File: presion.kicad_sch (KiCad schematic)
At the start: 7 parts, among them J6 Sens. Presión, U7 LM358

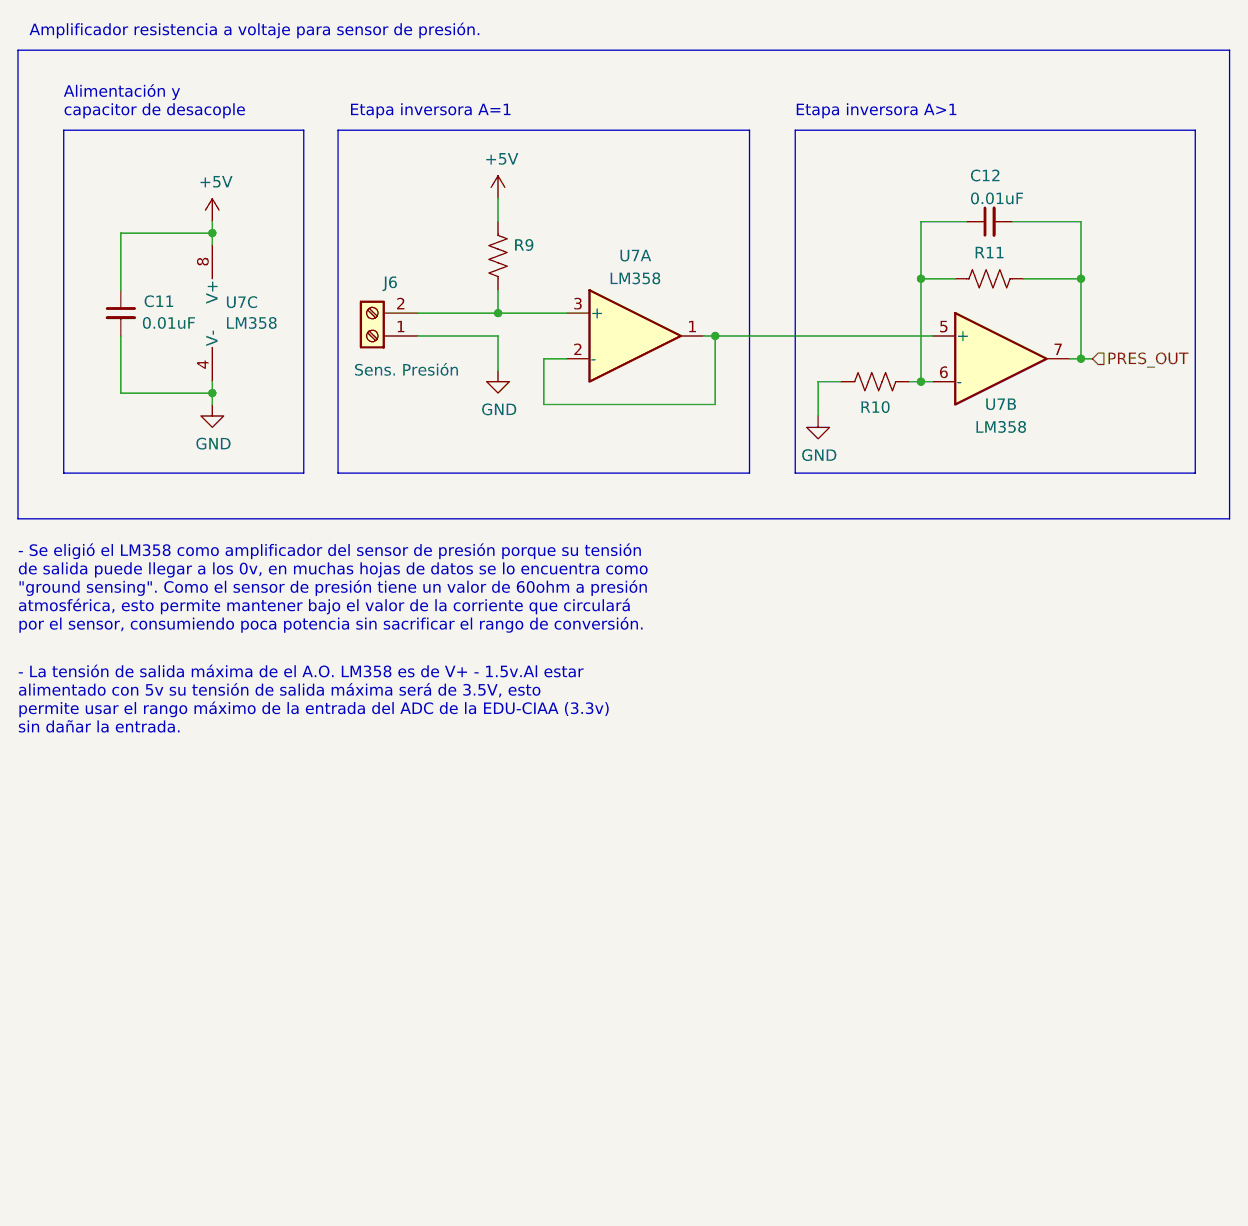
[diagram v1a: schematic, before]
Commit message: Cambios en plano de presion y agregue render en 3D de la placa.
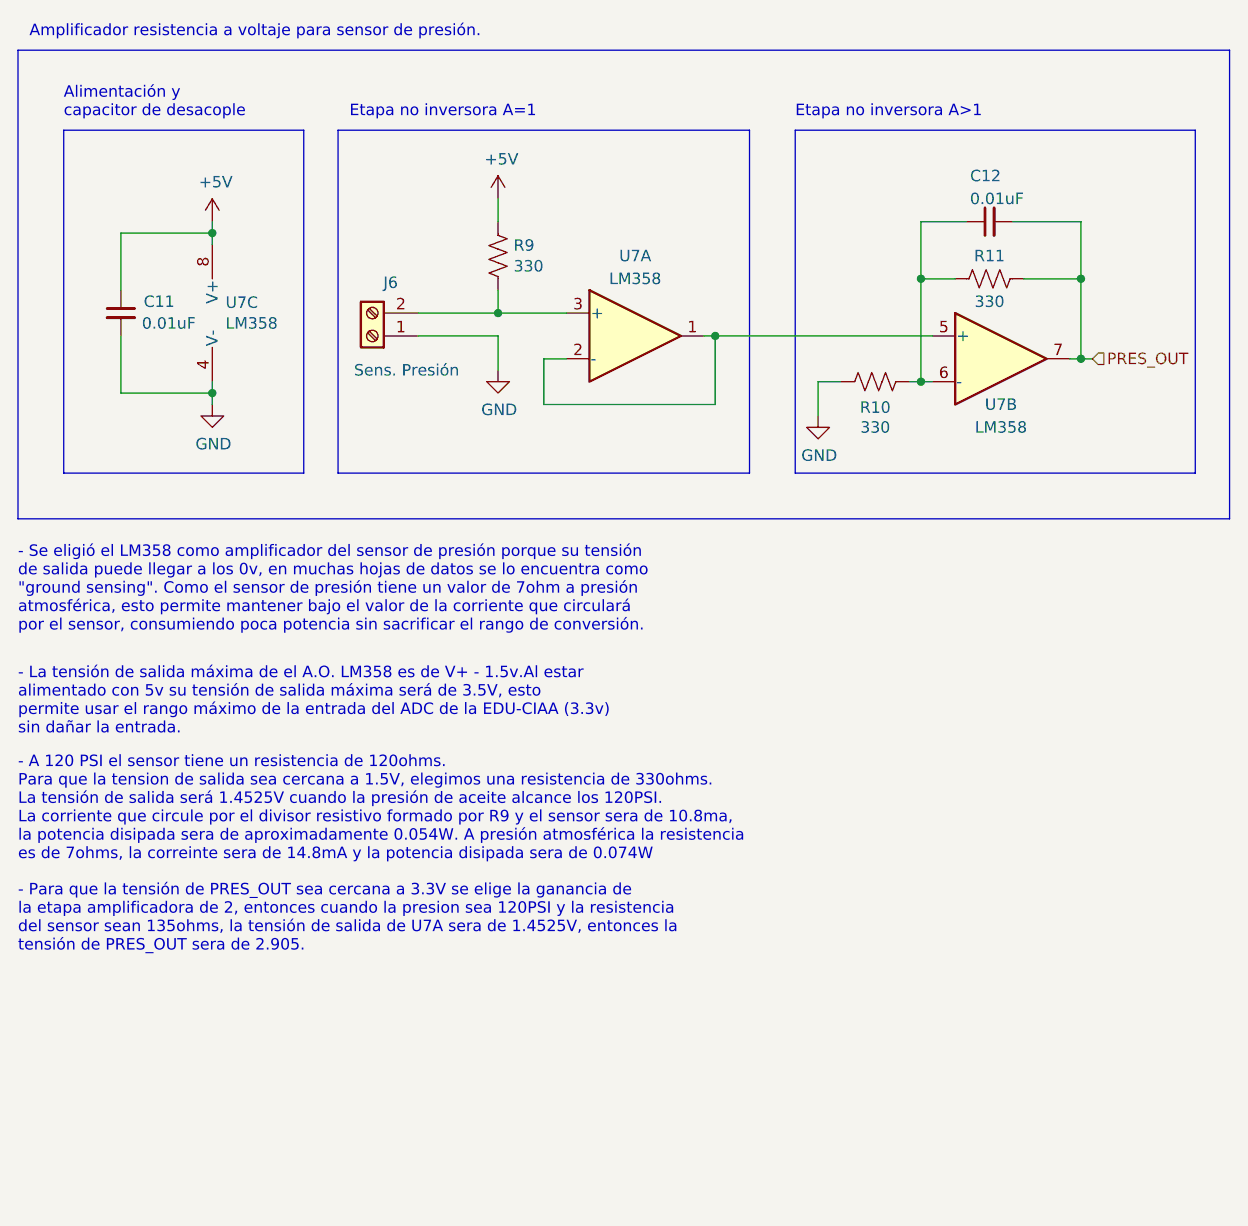
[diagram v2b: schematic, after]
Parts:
- R10, R11, R9: value R_US -> 330
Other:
- note added: "- A 120 PSI el sensor tiene un resistencia de 120ohms. Para que la tension de salida sea cercana a 1.5V, elegimos una resistencia de 330ohms. La tensión de salida será 1.4525V cuando la presión de aceite alcance los 120PSI. La corriente que circule por el divisor resistivo formado por R9 y el sensor sera de 10.8ma, la potencia disipada sera de aproximadamente 0.054W. A presión atmosférica la resi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"
- note added: "- Para que la tensión de PRES_OUT sea cercana a 3.3V se elige la ganancia de la etapa amplificadora de 2, entonces cuando la presion sea 120PSI y la resistencia del sensor sean 135ohms, la tensión de salida de U7A sera de 1.4525V, entonces la tensión de PRES_OUT sera de 2.905."
- note added: "- Se eligió el LM358 como amplificador del sensor de presión porque su tensión de salida puede llegar a los 0v, en muchas hojas de datos se lo encuentra como "ground sensing". Como el sensor de presión tiene un valor de 7ohm a presión atmosférica, esto permite mantener bajo el valor de la corriente que circulará por el sensor, consumiendo poca potencia sin sacrificar el rango de conversión."
- note added: "Etapa no inversora A=1"
- note added: "Etapa no inversora A>1"
- note removed: "- Se eligió el LM358 como amplificador del sensor de presión porque su tensión de salida puede llegar a los 0v, en muchas hojas de datos se lo encuentra como "ground sensing". Como el sensor de presión tiene un valor de 60ohm a presión atmosférica, esto permite mantener bajo el valor de la corriente que circulará por el sensor, consumiendo poca potencia sin sacrificar el rango de conversión."
- note removed: "Etapa inversora A=1"
- note removed: "Etapa inversora A>1"
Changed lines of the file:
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@@
     (stroke (width 0) (type default))
   )
-  (text "Etapa inversora A>1" (at 124.46 113.03 0)
+  (text "Etapa no inversora A>1" (at 124.46 113.03 0)
     (effects (font (size 1.27 1.27)) (justify left bottom))
   )
@@
     (effects (font (size 1.27 1.27)) (justify left bottom))
   )
-  (text "Etapa inversora A=1" (at 74.93 113.03 0)
-    (effects (font (size 1.27 1.27)) (justify left bottom))
-  )
-  (text "- Se eligió el LM358 como amplificador del sensor de presión porque su tensión\nde salida puede llegar a los 0v, en muchas hojas de datos se lo encuentra como\n\"ground sensing\". Como el sensor de presión tiene un valor de 60ohm a presión\natmosférica, esto permite mantener bajo el valor de la corriente que circulará\npor el sensor, consumiendo poca potencia sin sacrificar el rango de conversión."
+  (text "Etapa no inversora A=1" (at 74.93 113.03 0)
+    (effects (font (size 1.27 1.27)) (justify left bottom))
+  )
+  (text "- Se eligió el LM358 como amplificador del sensor de presión porque su tensión\nde salida puede llegar a los 0v, en muchas hojas de datos se lo encuentra como\n\"ground sensing\". Como el sensor de presión tiene un valor de 7ohm a presión\natmosférica, esto permite mantener bajo el valor de la corriente que circulará\npor el sensor, consumiendo poca potencia sin sacrificar el rango de conversión."
     (at 38.1 170.18 0)
     (effects (font (size 1.27 1.27)) (justify left bottom))
@@
   )
   (text "Alimentación y\ncapacitor de desacople" (at 43.18 113.03 0)
+    (effects (font (size 1.27 1.27)) (justify left bottom))
+  )
+  (text "- A 120 PSI el sensor tiene un resistencia de 120ohms.\nPara que la tension de salida sea cercana a 1.5V, elegimos una resistencia de 330ohms.\nLa tensión de salida será 1.4525V cuando la presión de aceite alcance los 120PSI.\nLa corriente que circule por el divisor resistivo formado por R9 y el sensor sera de 10.8ma,\nla potencia disipada sera de aproximadamente 0.054W. A presión atmosférica la resistencia \nes de 7ohms, la correinte sera de 14.8mA y la potencia disipada sera de 0.074W"
+    (at 38.1 195.58 0)
+    (effects (font (size 1.27 1.27)) (justify left bottom))
+  )
+  (text "- Para que la tensión de PRES_OUT sea cercana a 3.3V se elige la ganancia de\nla etapa amplificadora de 2, entonces cuando la presion sea 120PSI y la resistencia\ndel sensor sean 135ohms, la tensión de salida de U7A sera de 1.4525V, entonces la\ntensión de PRES_OUT sera de 2.905."
+    (at 38.1 205.74 0)
     (effects (font (size 1.27 1.27)) (justify left bottom))
   )
@@
       (effects (font (size 1.27 1.27)) (justify left))
     )
-    (property "Value" "R_US" (at 93.1672 129.413 0)
-      (effects (font (size 1.27 1.27)) (justify left) hide)
+    (property "Value" "330" (at 93.1672 129.413 0)
+      (effects (font (size 1.27 1.27)) (justify left))
     )
     (property "Footprint" "Resistor_SMD:R_0805_2012Metric_Pad1.15x1.40mm_HandSolder" (at 92.456 128.524 90)
@@
       (effects (font (size 1.27 1.27)))
     )
-    (property "Value" "R_US" (at 133.35 145.1356 0)
-      (effects (font (size 1.27 1.27)) hide)
+    (property "Value" "330" (at 133.35 147.32 90)
+      (effects (font (size 1.27 1.27)))
     )
     (property "Footprint" "Resistor_SMD:R_0805_2012Metric_Pad1.15x1.40mm_HandSolder" (at 133.604 141.224 90)
@@
   (symbol (lib_id "Device:R_US") (at 146.05 130.81 270) (unit 1)
     (in_bom yes) (on_board yes) (dnp no)
-    (property "Reference" "R11" (at 146.05 127.9398 90)
-      (effects (font (size 1.27 1.27)))
-    )
-    (property "Value" "R_US" (at 146.05 127.9144 0)
-      (effects (font (size 1.27 1.27)) hide)
+    (property "Reference" "R11" (at 146.05 128.27 90)
+      (effects (font (size 1.27 1.27)))
+    )
+    (property "Value" "330" (at 146.05 133.35 90)
+      (effects (font (size 1.27 1.27)))
     )
     (property "Footprint" "Resistor_SMD:R_0805_2012Metric_Pad1.15x1.40mm_HandSolder" (at 145.796 131.826 90)

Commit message: Agregué datos sobre función transferencia del circuito de presión.
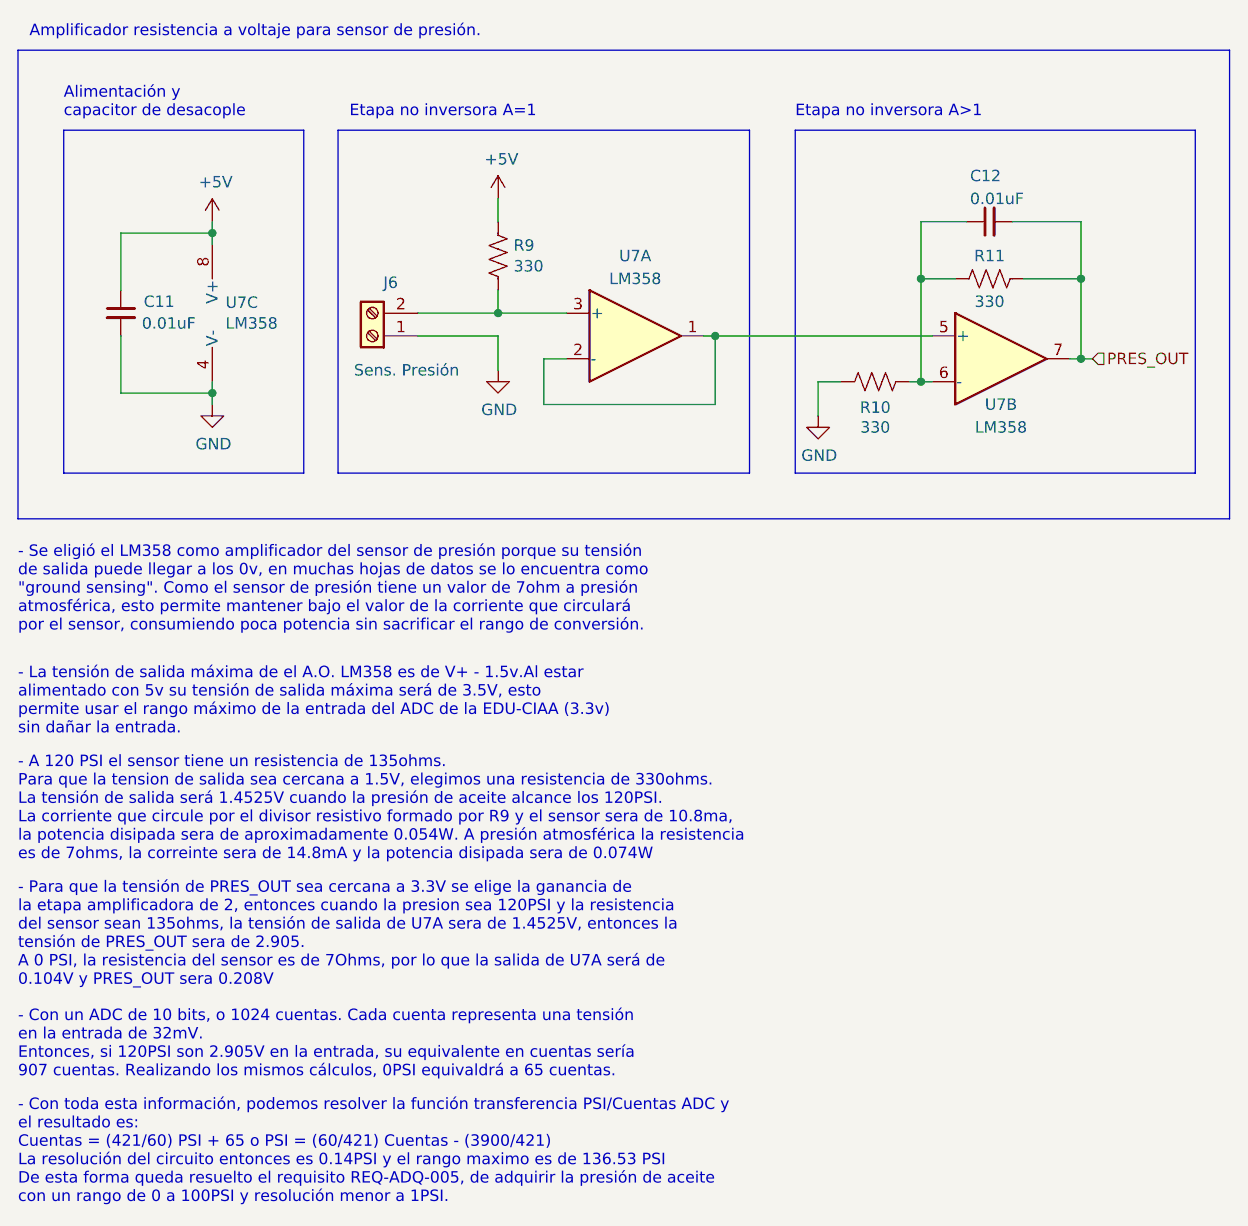
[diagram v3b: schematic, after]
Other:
- note added: "- A 120 PSI el sensor tiene un resistencia de 135ohms. Para que la tension de salida sea cercana a 1.5V, elegimos una resistencia de 330ohms. La tensión de salida será 1.4525V cuando la presión de aceite alcance los 120PSI. La corriente que circule por el divisor resistivo formado por R9 y el sensor sera de 10.8ma, la potencia disipada sera de aproximadamente 0.054W. A presión atmosférica la resi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"
- note added: "- Con toda esta información, podemos resolver la función transferencia PSI/Cuentas ADC y el resultado es: Cuentas = (421/60) PSI + 65 o PSI = (60/421) Cuentas - (3900/421) La resolución del circuito entonces es 0.14PSI y el rango maximo es de 136.53 PSI De esta forma queda resuelto el requisito REQ-ADQ-005, de adquirir la presión de aceite con un rango de 0 a 100PSI y resolución menor a 1PSI."
- note added: "- Con un ADC de 10 bits, o 1024 cuentas. Cada cuenta representa una tensión en la entrada de 32mV. Entonces, si 120PSI son 2.905V en la entrada, su equivalente en cuentas sería 907 cuentas. Realizando los mismos cálculos, 0PSI equivaldrá a 65 cuentas."
- note added: "- Para que la tensión de PRES_OUT sea cercana a 3.3V se elige la ganancia de la etapa amplificadora de 2, entonces cuando la presion sea 120PSI y la resistencia del sensor sean 135ohms, la tensión de salida de U7A sera de 1.4525V, entonces la tensión de PRES_OUT sera de 2.905. A 0 PSI, la resistencia del sensor es de 7Ohms, por lo que la salida de U7A será de 0.104V y PRES_OUT sera 0.208V"
- note removed: "- A 120 PSI el sensor tiene un resistencia de 120ohms. Para que la tension de salida sea cercana a 1.5V, elegimos una resistencia de 330ohms. La tensión de salida será 1.4525V cuando la presión de aceite alcance los 120PSI. La corriente que circule por el divisor resistivo formado por R9 y el sensor sera de 10.8ma, la potencia disipada sera de aproximadamente 0.054W. A presión atmosférica la resi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"
- note removed: "- Para que la tensión de PRES_OUT sea cercana a 3.3V se elige la ganancia de la etapa amplificadora de 2, entonces cuando la presion sea 120PSI y la resistencia del sensor sean 135ohms, la tensión de salida de U7A sera de 1.4525V, entonces la tensión de PRES_OUT sera de 2.905."
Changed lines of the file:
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@@
+    (effects (font (size 1.27 1.27)) (justify left bottom))
+  )
+  (text "- Con un ADC de 10 bits, o 1024 cuentas. Cada cuenta representa una tensión\nen la entrada de 32mV.\nEntonces, si 120PSI son 2.905V en la entrada, su equivalente en cuentas sería\n907 cuentas. Realizando los mismos cálculos, 0PSI equivaldrá a 65 cuentas."
+    (at 38.1 219.71 0)
+    (effects (font (size 1.27 1.27)) (justify left bottom))
+  )
+  (text "- Con toda esta información, podemos resolver la función transferencia PSI/Cuentas ADC y\nel resultado es:\nCuentas = (421/60) PSI + 65 o PSI = (60/421) Cuentas - (3900/421)\nLa resolución del circuito entonces es 0.14PSI y el rango maximo es de 136.53 PSI\nDe esta forma queda resuelto el requisito REQ-ADQ-005, de adquirir la presión de aceite \ncon un rango de 0 a 100PSI y resolución menor a 1PSI.\n"
+    (at 38.1 233.68 0)
     (effects (font (size 1.27 1.27)) (justify left bottom))
   )
@@
     (effects (font (size 1.27 1.27)) (justify left bottom))
   )
-  (text "- A 120 PSI el sensor tiene un resistencia de 120ohms.\nPara que la tension de salida sea cercana a 1.5V, elegimos una resistencia de 330ohms.\nLa tensión de salida será 1.4525V cuando la presión de aceite alcance los 120PSI.\nLa corriente que circule por el divisor resistivo formado por R9 y el sensor sera de 10.8ma,\nla potencia disipada sera de aproximadamente 0.054W. A presión atmosférica la resistencia \nes de 7ohms, la correinte sera de 14.8mA y la potencia disipada sera de 0.074W"
+  (text "- A 120 PSI el sensor tiene un resistencia de 135ohms.\nPara que la tension de salida sea cercana a 1.5V, elegimos una resistencia de 330ohms.\nLa tensión de salida será 1.4525V cuando la presión de aceite alcance los 120PSI.\nLa corriente que circule por el divisor resistivo formado por R9 y el sensor sera de 10.8ma,\nla potencia disipada sera de aproximadamente 0.054W. A presión atmosférica la resistencia \nes de 7ohms, la correinte sera de 14.8mA y la potencia disipada sera de 0.074W"
     (at 38.1 195.58 0)
     (effects (font (size 1.27 1.27)) (justify left bottom))
   )
-  (text "- Para que la tensión de PRES_OUT sea cercana a 3.3V se elige la ganancia de\nla etapa amplificadora de 2, entonces cuando la presion sea 120PSI y la resistencia\ndel sensor sean 135ohms, la tensión de salida de U7A sera de 1.4525V, entonces la\ntensión de PRES_OUT sera de 2.905."
-    (at 38.1 205.74 0)
+  (text "- Para que la tensión de PRES_OUT sea cercana a 3.3V se elige la ganancia de\nla etapa amplificadora de 2, entonces cuando la presion sea 120PSI y la resistencia\ndel sensor sean 135ohms, la tensión de salida de U7A sera de 1.4525V, entonces la\ntensión de PRES_OUT sera de 2.905.\nA 0 PSI, la resistencia del sensor es de 7Ohms, por lo que la salida de U7A será de\n0.104V y PRES_OUT sera 0.208V"
+    (at 38.1 209.55 0)
     (effects (font (size 1.27 1.27)) (justify left bottom))
   )
